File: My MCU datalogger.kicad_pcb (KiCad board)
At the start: 2 copper layers, 29 parts, among them J1 Conn_01x04_Male, J2 Conn_01x09_Male, J3 Conn_01x04_Male, J4 Conn_02x03_Odd_Even, U1 24LC1025, U2 DS1307Z, U3 24LC1025, U4 ATMEGA328P-AU, Y1 32.768 KHz, Y2 16 MHz

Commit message: Initial layout
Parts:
- moved H4 95.9 mm to (86.4, 111.2)
- moved J2 94.9 mm to (45.1, 111.1), turned to 90 degrees
- moved J3 90.6 mm to (70.5, 111.1), turned to 90 degrees
- moved Y2 85.4 mm to (63.5, 104.8)
- moved C4 82.3 mm to (72.2, 106.0)
- moved C2 77.4 mm to (72.2, 102.2)
- moved J1 76.9 mm to (84.5, 99.1)
- moved H2 76.4 mm to (40.6, 111.2)
- moved R6 73.7 mm to (77.2, 94.0)
- moved R2 73.6 mm to (52.4, 106.7)
- moved R1 70.8 mm to (48.3, 106.7)
- moved H3 70.4 mm to (86.4, 85.8)
- moved R4 70.3 mm to (72.3, 94.0)
- moved R3 66.8 mm to (72.3, 98.4)
- moved D2 65.4 mm to (72.3, 85.7)
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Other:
- board outline added: 50.8 x 30.5 mm

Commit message: Outline refinement
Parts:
- moved J2 63.3 mm to (43.4, 47.8)
- moved J3 63.3 mm to (68.8, 47.8)
- moved C4 62.8 mm to (68.2, 43.4)
- moved Y1 62.6 mm to (41.5, 40.8)
- moved C2 62.5 mm to (68.2, 39.9)
- moved R3 62.1 mm to (68.2, 36.5)
- moved H3 61.7 mm to (81.5, 24.3)
- moved H4 61.7 mm to (81.5, 49.7)
- moved J1 61.6 mm to (79.6, 37.7)
- moved J4 61.6 mm to (77.1, 28.8)
- moved Y2 61.6 mm to (59.3, 43.4)
- moved H1 61.5 mm to (39.0, 24.3)
- moved H2 61.5 mm to (39.0, 49.7)
- moved BT1 61.4 mm to (41.5, 29.4)
- moved R1 61.4 mm to (46.6, 45.3)
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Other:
- board size 50.8 x 30.5 mm -> 47.6 x 30.5 mm

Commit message: Final outline
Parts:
- moved U4 0.58 mm to (59.5, 34.3)
- turned Y2 to 180 degrees
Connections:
- U4 pad 12: /DB -> /D8
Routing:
- net /Vcc: track 0.00 -> 197.1 mm, vias 0 -> 12
- net /SCK: track 0.00 -> 89.4 mm, vias 0 -> 6
- net GND: track 0.00 -> 77.2 mm, vias 0 -> 16
- net /SDA: track 0.00 -> 67.5 mm, vias 0 -> 6
- net /MOSI: track 0.00 -> 37.9 mm
- net /RESET: track 0.00 -> 37.6 mm, vias 0 -> 4
- net /TX: track 0.00 -> 36.6 mm, vias 0 -> 2
- net Net-(C2-Pad2): track 0.00 -> 31.9 mm, vias 0 -> 2
- net Net-(C3-Pad2): track 0.00 -> 31.8 mm, vias 0 -> 2
- net /D2: track 0.00 -> 28.8 mm
- net /RX: track 0.00 -> 27.6 mm, vias 0 -> 1
- net /D5: track 0.00 -> 27.3 mm
- net /D6: track 0.00 -> 24.8 mm
- net /D7: track 0.00 -> 23.2 mm
- net /D3: track 0.00 -> 22.7 mm
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- added copper zone on B.Cu, net GND

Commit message: Finalized
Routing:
- net /Vcc: track 197.1 -> 184.8 mm
- net GND: track 77.2 -> 66.0 mm, vias 16 -> 13
- net /SCK: track 89.4 -> 83.4 mm
- net /MOSI: track 37.9 -> 33.8 mm
- net /TX: track 36.6 -> 33.5 mm
- net /RESET: track 37.6 -> 34.6 mm
- net /D8: track 9.93 -> 12.8 mm
- net Net-(R2-Pad2): track 8.96 -> 6.21 mm
- net /SDA: track 67.5 -> 65.0 mm
- net Net-(D1-Pad2): track 22.0 -> 19.7 mm
- net /D7: track 23.2 -> 22.4 mm
- net /D5: track 27.3 -> 26.6 mm
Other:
- board size 47.6 x 30.5 mm -> 47.7 x 30.6 mm

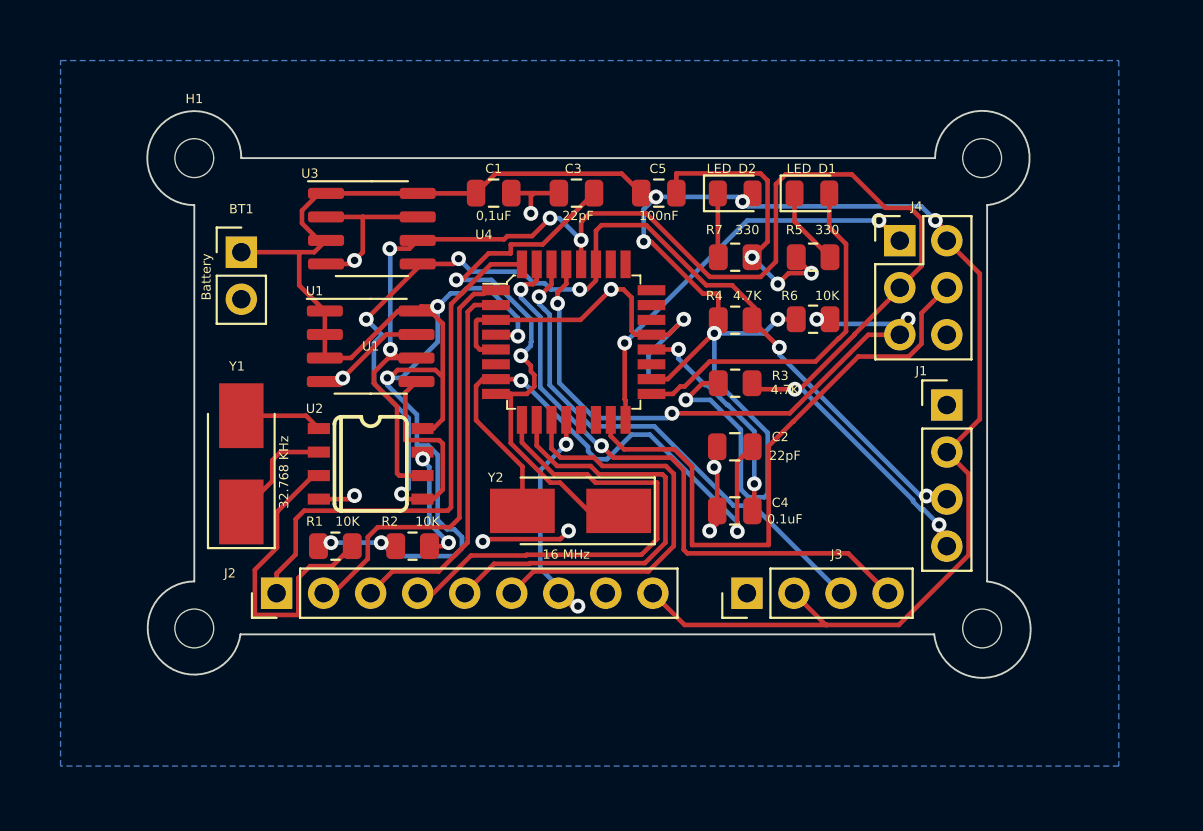
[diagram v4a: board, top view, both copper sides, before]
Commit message: Added front filled zone for Vcc net
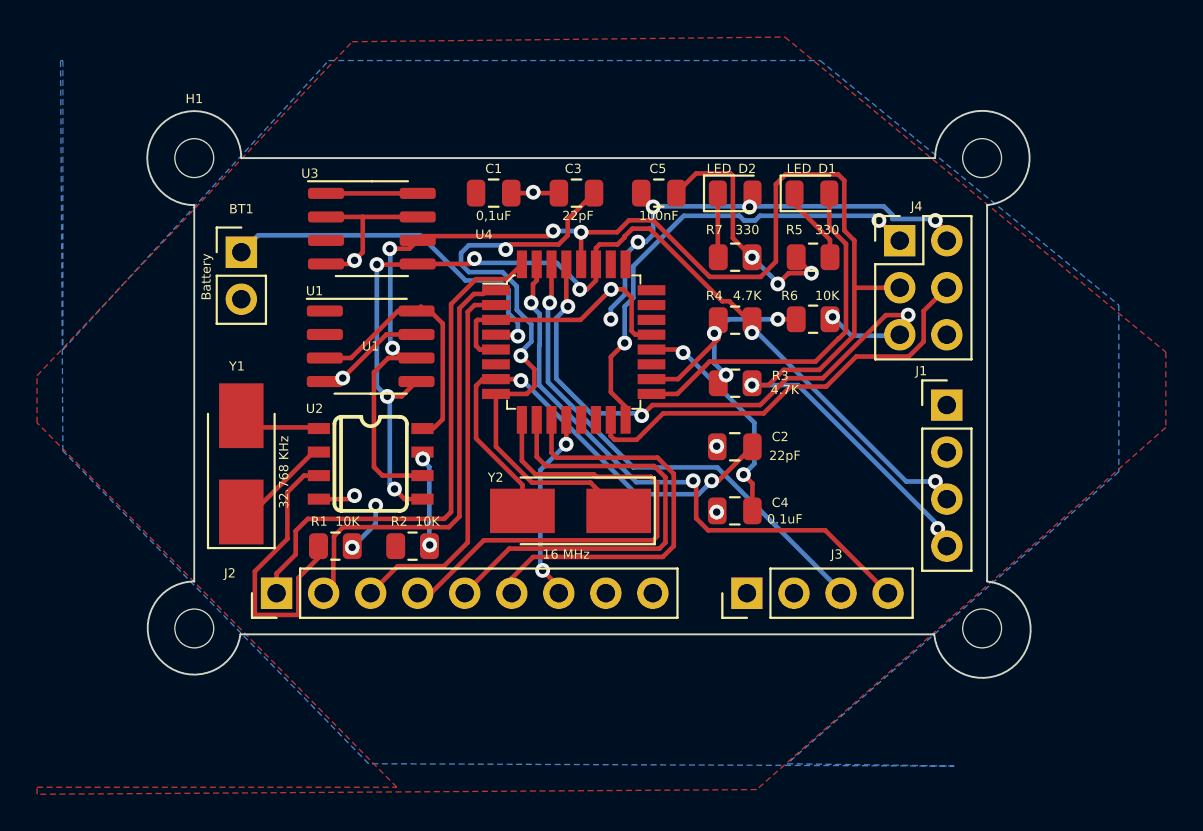
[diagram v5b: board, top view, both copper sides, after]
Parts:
- turned R1 to 180 degrees
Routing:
- net /Vcc: track 184.8 -> 81.9 mm, vias 12 -> 11
- net GND: track 66.0 -> 48.2 mm, vias 13 -> 10
- net /MOSI: track 33.8 -> 23.5 mm
- net /SDA: track 65.0 -> 56.9 mm, vias 6 -> 7
- net Net-(C2-Pad2): track 31.9 -> 26.5 mm
- net /MISO: track 22.2 -> 25.4 mm
- net /D8: track 12.8 -> 10.4 mm
- net /TX: track 33.5 -> 31.5 mm
- net Net-(R1-Pad2): track 17.1 -> 15.3 mm
- net Net-(R2-Pad2): track 6.21 -> 4.87 mm
- net Net-(C3-Pad2): track 31.8 -> 32.7 mm
- net /D3: track 22.7 -> 23.4 mm
- net Net-(U2-Pad2): track 6.18 -> 5.53 mm
- net /D7: track 22.4 -> 23.0 mm
- net /SCK: track 83.4 -> 82.9 mm
- added copper zone on F.Cu, net /Vcc

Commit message: Routing improvements
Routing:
- net /Vcc: track 81.9 -> 96.5 mm, vias 11 -> 8
- net /RESET: track 35.0 -> 30.7 mm
- net /MISO: track 25.4 -> 22.4 mm
- net /SDA: track 56.9 -> 54.6 mm
- net Net-(C4-Pad2): track 12.4 -> 11.2 mm
- net Net-(D1-Pad2): track 19.7 -> 20.8 mm
- net Net-(C3-Pad2): track 32.7 -> 31.8 mm
- net /MOSI: track 23.5 -> 24.0 mm
- net Net-(C2-Pad2): track 26.5 -> 27.0 mm

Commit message: Generated Gerbers files
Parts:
- added G***: LOGO, 4x8x8 matrix display:TE_Logo_11.6x4, B.Cu at (64.5, 75.2)
- added REF**: KiCad-Logo2_5mm_SilkScreen, Symbol:KiCad-Logo2_5mm_SilkScreen, B.Cu at (55.9, 60.7)
- moved C2 33.6 mm to (74.2, 73.0)
- moved H2 33.6 mm to (45.1, 82.8)
- moved H4 33.6 mm to (87.6, 82.8)
- moved J1 33.6 mm to (85.7, 70.7)
- moved R3 33.6 mm to (74.3, 69.5)
- moved R4 33.6 mm to (74.3, 66.1)
- moved U2 33.6 mm to (54.6, 73.9)
- moved Y1 33.6 mm to (47.6, 73.9)
- moved BT1 33.6 mm to (47.6, 62.4)
- moved C1 33.6 mm to (61.2, 59.3)
- moved C3 33.6 mm to (65.7, 59.3)
- moved C5 33.6 mm to (70.1, 59.3)
- moved D1 33.6 mm to (78.4, 59.3)
- moved D2 33.6 mm to (74.3, 59.3)
- moved H1 33.6 mm to (45.1, 57.4)
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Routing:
- net Net-(R1-Pad2): track 15.3 -> 16.0 mm
- net /D2: track 28.5 -> 27.8 mm
- net /TX: track 31.8 -> 31.2 mm
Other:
- board text added: "0.2000 mm / 0.0000 mm"
- board text added: "0.3000 mm"
- board text added: "1.6000 mm"
- board text added: "2"
- board text added: "47.7044 mm x 30.6182 mm"
- board text added: "BOARD CHARACTERISTICS"
- board text added: "Board Thickness:"
- board text added: "Board overall dimensions:"
- board text added: "Castellated pads:"
- board text added: "Copper Finish:"
- board text added: "Copper Layer Count:"
- board text added: "Data logger with the ATMega328P. - 2Mbit EEPROM - RTC - I2C, SPI, GPIOs"
- board text added: "Edge card connectors:"
- board text added: "Impedance Control:"
- board text added: "Min hole diameter:"
- board text added: "Min track/spacing:"
- board text added: "No"
- board text added: "None"
- board text added: "PCB V. ${design_version}"
- board text added: "Plated Board Edge:"

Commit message: 4_layers final candidate
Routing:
- net /Vcc: track 96.3 -> 9.59 mm, vias 8 -> 17
- net GND: track 48.0 -> 7.26 mm, vias 10 -> 12
- net Net-(C2-Pad2): track 27.0 -> 44.4 mm, vias 2 -> 0
- net Net-(R1-Pad2): track 16.0 -> 4.56 mm
- net /SCK: track 83.1 -> 71.8 mm, vias 6 -> 2
- net /D5: track 27.1 -> 16.3 mm
- net /D6: track 24.9 -> 14.1 mm
- net /RESET: track 30.7 -> 22.7 mm, vias 4 -> 2
- net /D7: track 23.0 -> 15.5 mm, vias 0 -> 1
- net Net-(C4-Pad2): track 11.2 -> 18.3 mm
- net Net-(C3-Pad2): track 31.8 -> 25.3 mm, vias 2 -> 4
- net /SDA: track 54.6 -> 60.8 mm, vias 7 -> 2
- net /TX: track 31.2 -> 37.3 mm, vias 2 -> 1
- net /D2: track 27.8 -> 24.0 mm, vias 0 -> 1
- net /MOSI: track 24.0 -> 22.4 mm, vias 0 -> 1
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- added copper zone on In1.Cu, net /Vcc
- added copper zone on F.Cu, net GND
- removed copper zone on F.Cu, net /Vcc
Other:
- copper layers 2 -> 4
